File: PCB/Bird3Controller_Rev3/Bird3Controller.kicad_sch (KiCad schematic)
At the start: 61 parts, among them IC1 M24C08-RMN6TP, IC2 AP63203WU-7, J1 Bird 3 24-pin Connector, J2 TXW154028S0 Connector, J3 87832-2220, Q1 2N7002A, SW1 SW_Boot, SW2 SW_Reset, U1 ESP32-S3-WROOM-1, U3 SN65HVD231, U4 LMR36520ADDAR, U5 LM3519MK-20_NOPB

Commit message: Rearrange schematic
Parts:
- J4: value ~ -> Adafruit USB-C Breakout
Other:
- moved on the sheet: C14, C15, C16, C17, C18, C19, C20, C21, C22, C4, C5, C6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

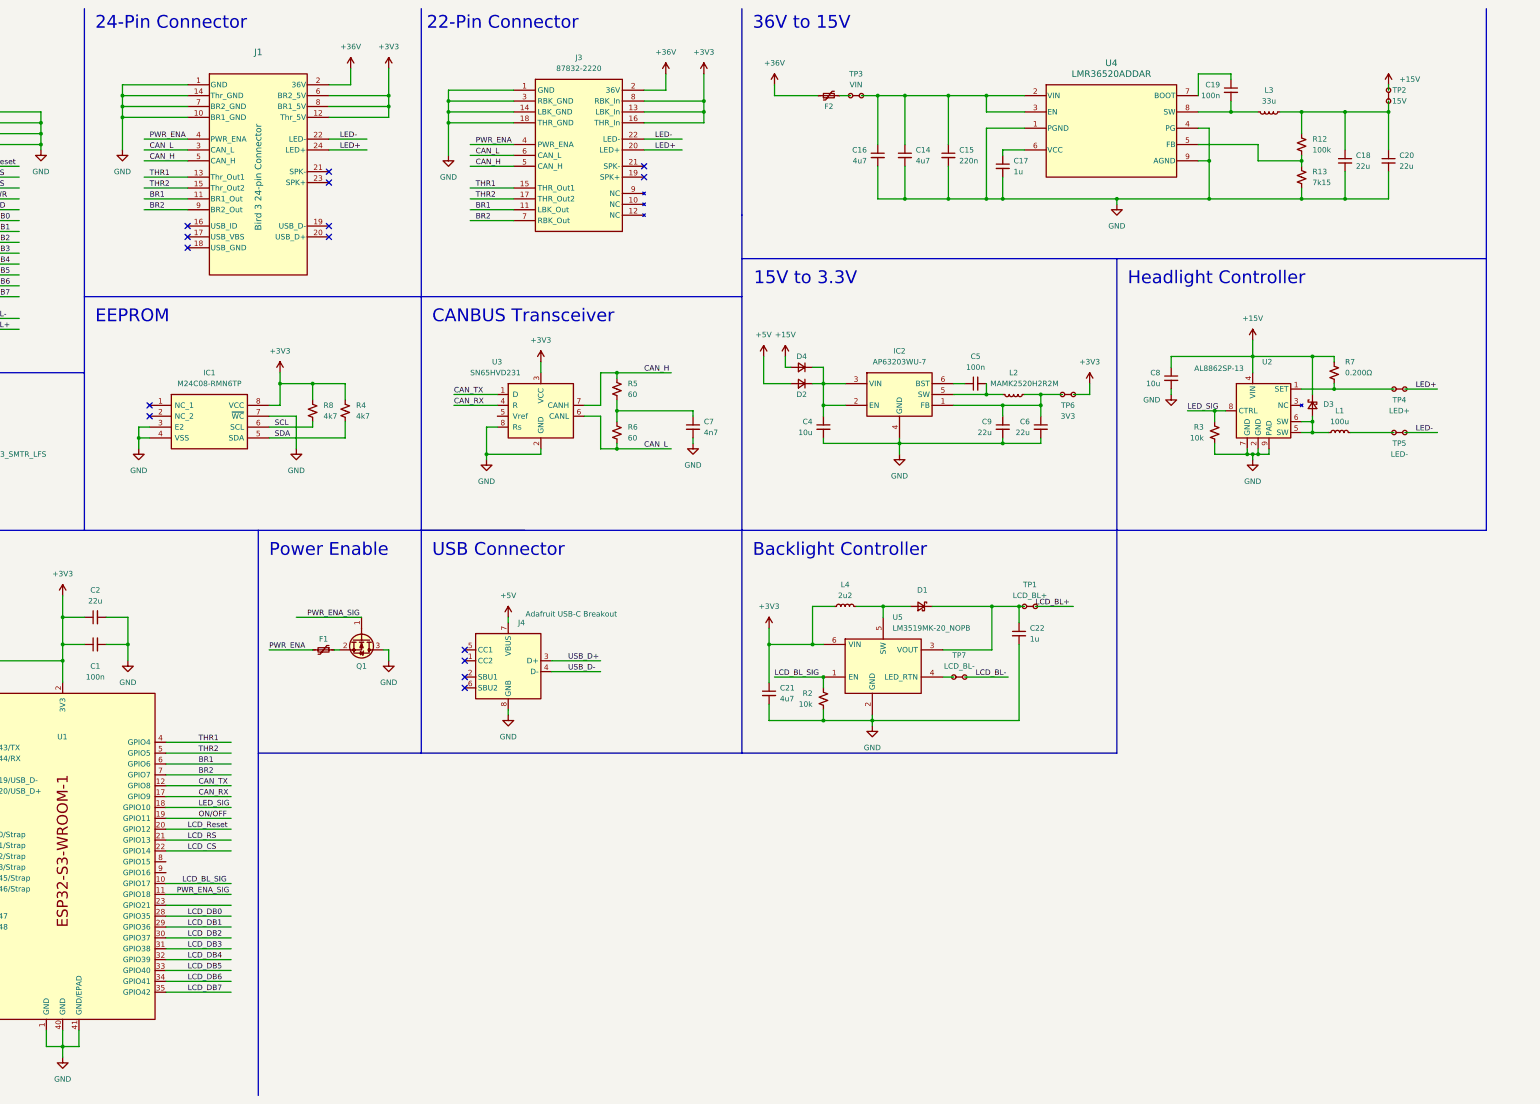
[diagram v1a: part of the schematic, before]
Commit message: Add test points
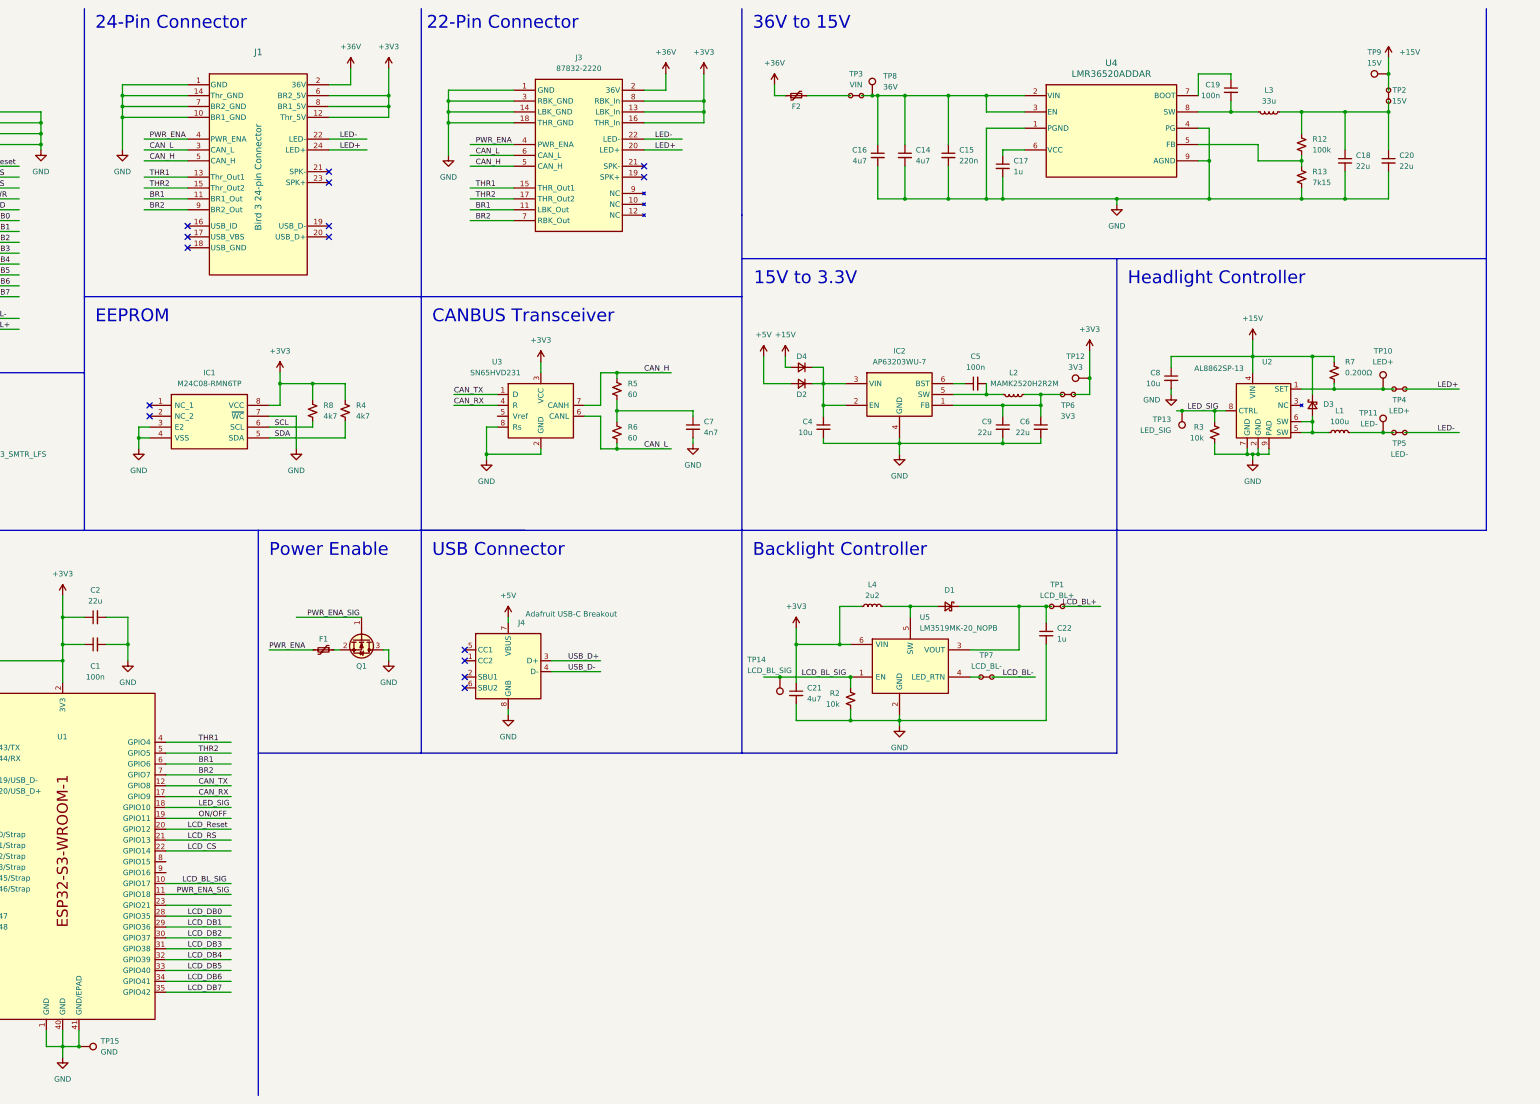
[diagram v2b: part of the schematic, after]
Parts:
- added TP10: LED+, Bird3Controller:Labeled_TestPoint_1.5mm, symbol Connector:TestPoint
- added TP11: LED-, Bird3Controller:Labeled_TestPoint_1.5mm, symbol Connector:TestPoint
- added TP12: 3V3, Bird3Controller:Labeled_TestPoint_1.5mm, symbol Connector:TestPoint
- added TP13: LED_SIG, Bird3Controller:Labeled_TestPoint_1.5mm, symbol Connector:TestPoint
- added TP14: LCD_BL_SIG, Bird3Controller:Labeled_TestPoint_1.5mm, symbol Connector:TestPoint
- added TP15: GND, Bird3Controller:Labeled_TestPoint_1.5mm, symbol Connector:TestPoint
- added TP8: 36V, Bird3Controller:Labeled_TestPoint_1.5mm, symbol Connector:TestPoint
- added TP9: 15V, Bird3Controller:Labeled_TestPoint_1.5mm, symbol Connector:TestPoint
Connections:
- net +15V: now also TP9.1
- net +3V3: now also TP12.1
- net GND: now also TP15.1
- net LCD_BL_SIG: now also TP14.1
- net LED_SIG: now also TP13.1
- net at R7.2, TP4.1, U2.1 (SET): now also TP10.1
- net at L1.2, TP5.1: now also TP11.1
- net at C14.1, C15.1, C16.1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: now also TP8.1
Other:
- moved on the sheet: C21, C22, D1, F2, L4, R2, TP1, TP7, U5

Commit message: Add `Rating` field, use lower cost VIN cap, add description to most components
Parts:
- C1, C17, C19, C22, C3, C5, C7: Rating (none) -> 50V
- C14, C16, C21: Mouser Part Number 187-CL32Y475MCIVPNE -> 187-CL32B475KBUYNNE; Mouser Price QTY1 0.68 -> 0.36; Mouser Price QTY10 0.475 -> 0.179; Mouser Price/Stock https://www.mouser.com/ProductDetail/Samsung-Electro-Mechanics/CL32Y475MCIVPNE?qs=Znm5pLBrcAJ2Wm3glbzndQ%3D%3D -> https://www.mouser.com/ProductDetail/Samsung-Electro-Mechanics/CL32B475KBUYNNE?qs=hqM3L16%252Bxlekel2U%252B66N8g%3D%3D; Rating (none) -> 50V
- C15: Manufacturer_Name KYOCERA AVX -> Samsung Electro-Mechanics; Manufacturer_Part_Number 08053C224K4T4A -> CL21B224KBFNNNG; Mouser Part Number 581-08053C224K4T4A -> 187-CL21B224KBFNNNG; Mouser Price QTY1 0.11 -> 0.10; Mouser Price QTY10 0.078 -> 0.02; Mouser Price/Stock https://www.mouser.com/ProductDetail/KYOCERA-AVX/08053C224K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 -> https://www.mouser.com/ProductDetail/Samsung-Electro-Mechan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; Rating (none) -> 50V
- C18, C20, C4, C8: Rating (none) -> 25V
- C2: Rating (none) -> 16V
- C6, C9: Rating (none) -> 6.3V
- D1, D3: Rating (none) -> 20V
- D2, D4: Rating (none) -> 600V
- F1, F2, U2: Rating (none) -> 60V
- IC1, U5: Rating (none) -> 5.5V
- IC2: Mouser Price QTY1 (none) -> 0.87; Mouser Price QTY10 (none) -> 0.71; Rating (none) -> 32V
- J1, J3: Rating (none) -> 125V, 2A
- J2: Rating (none) -> 50V, 125mA
- L1: Rating (none) -> 1.2A, 300mOhms
- L2: value MAMK2520H2R2M -> 2u2; Mouser Price QTY1 (none) -> 0.23; Mouser Price QTY10 (none) -> 0.158; Rating (none) -> 2.2A, 90mOhms
- L3: Rating (none) -> 4A, 127.6mOhms
- L4: Rating (none) -> 1.3A, 80mOhms
- Q1: Rating (none) -> 60V, 280mA, 2 Ohms
- R1, R2, R3, R4, R8: Rating (none) -> 150v, 125mW
- R12, R13, R5, R6: Rating (none) -> 150v, 500mW
- R7: Rating (none) -> 125mW
- S1, SW1, SW2: Rating (none) -> 12V, 50mA
- U1, U3: Rating (none) -> 3.6V
- U4: Rating (none) -> 65V

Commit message: Rename fields to work with `kicost`. Also, correct the Mouser Part Number for C15.
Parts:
- C1, C19, C3, C5: Manufacturer_Name YAGEO -> (none); Manufacturer_Part_Number AC0805JRX7R9BB104 -> (none); Mouser Part Number 603-AC0805JX7R9BB104 -> (none); Mouser Price QTY10 0.065 -> 0.037; Mouser Price/Stock https://www.mouser.com/ProductDetail/YAGEO/AC0805JRX7R9BB10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 -> https://www.mouser.com/ProductDetail/KYOCERA-AVX/KGM21NR71H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; manf (none) -> KYOCERA AVX; manf# (none) -> KGM21NR71H104KT; mouser# (none) -> 581-KGM21NR71H104KT
- C14, C16: Manufacturer_Name Samsung Electro-Mechanics -> (none); Manufacturer_Part_Number CL32Y475MCIVPNE -> (none); Mouser Part Number 187-CL32B475KBUYNNE -> (none); manf (none) -> Samsung Electro-Mechanics; manf# (none) -> CL21B105KBFNNNE; mouser# (none) -> 187-CL32B475KBUYNNE
- C15: Manufacturer_Name Samsung Electro-Mechanics -> (none); Manufacturer_Part_Number CL21B224KBFNNNG -> (none); Mouser Part Number 187-CL21B224KBFNNNG -> (none); manf (none) -> Samsung Electro-Mechanics; manf# (none) -> CL21B224KBFNNNG; mouser# (none) -> 187-CL21B224KBFNNNG
- C17, C22: Manufacturer_Name Samsung Electro-Mechanics -> (none); Manufacturer_Part_Number CL21B105MBFNNNE -> (none); Mouser Part Number 187-CL21B105MBFNNNE -> (none); Mouser Price QTY1 0.10 -> 0.11; Mouser Price QTY10 0.027 -> 0.045; Mouser Price/Stock https://www.mouser.com/ProductDetail/Samsung-Electro-Mechanics/CL21B105MBFNNNE?qs=Znm5pLBrcAIRYa0zX3s5Qw%3D%3D -> https://www.mouser.com/ProductDetail/Samsung-Electro-Mechanics/CL21B105KBFNNNE?qs=yOVawPpwOwmddQEBPU6Y9A%3D%3D; manf (none) -> Samsung Electro-Mechanics; manf# (none) -> CL21B105KBFNNNE; mouser# (none) -> 187-CL21B105KBFNNNE
- C18, C20: Manufacturer_Name Samsung Electro-Mechanics -> (none); Manufacturer_Part_Number CL21A226MAYNNNE -> (none); Mouser Part Number 187-CL21A226MAYNNNE -> (none); Mouser Price QTY1 0.25 -> 0.32; Mouser Price QTY10 0.115 -> 0.145; manf (none) -> Samsung Electro-Mechanics; manf# (none) -> CL21A226MAYNNWE; mouser# (none) -> 187-CL21A226MAYNNWE
- C2: Manufacturer_Name Murata Electronics -> (none); Manufacturer_Part_Number GRT21BR61C226ME13L -> (none); Mouser Part Number 81-GRT21BR61C226ME3L -> (none); manf (none) -> Murata Electronics; manf# (none) -> GRT21BR61C226ME13L; mouser# (none) -> 81-GRT21BR61C226ME3L
- C21: Manufacturer_Name Samsung Electro-Mechanics -> (none); Manufacturer_Part_Number CL32Y475MCIVPNE -> (none); Mouser Part Number 187-CL32B475KBUYNNE -> (none); manf (none) -> Samsung Electro-Mechanics; manf# (none) -> CL32B475KBUYNNE; mouser# (none) -> 187-CL32B475KBUYNNE
- C4, C8: Manufacturer_Name Murata Electronics -> (none); Manufacturer_Part_Number GRT21BC71E106KE13L -> (none); Mouser Part Number 81-GRT21BC71E106KE13 -> (none); manf (none) -> Murata Electronics; manf# (none) -> GRT21BC71E106KE13L; mouser# (none) -> 81-GRT21BC71E106KE13
- C6, C9: Manufacturer_Name Samsung Electro-Mechanics -> (none); Manufacturer_Part_Number CL21A226MQQNNNE -> (none); Mouser Part Number 187-CL21A226MQQNNNE -> (none); manf (none) -> Samsung Electro-Mechanics; manf# (none) -> CL21A226MQQNNNE; mouser# (none) -> 187-CL21A226MQQNNNE
- C7: Manufacturer_Name KYOCERA AVX -> (none); Manufacturer_Part_Number 08055C472K4T4A -> (none); Mouser Part Number 581-08055C472K4T4A -> (none); manf (none) -> KYOCERA AVX; manf# (none) -> 08055C472K4T4A; mouser# (none) -> 581-08055C472K4T4A
- D1, D3: Manufacturer_Name KYOCERA AVX -> (none); Manufacturer_Part_Number SD0805S020S1R0 -> (none); Mouser Part Number 581-SD0805S020S1R0 -> (none); manf (none) -> KYOCERA AVX; manf# (none) -> SD0805S020S1R0; mouser# (none) -> 581-SD0805S020S1R0
- D2, D4: Manufacturer_Name PANJIT -> (none); Manufacturer_Part_Number GS1J_R1_00001 -> (none); Mouser Part Number 241-GS1J_R1_00001 -> (none); manf (none) -> PANJIT; manf# (none) -> GS1J_R1_00001; mouser# (none) -> 241-GS1J_R1_00001
- F1: Manufacturer_Name Bel Fuse -> (none); Manufacturer_Part_Number 0ZCM0001FF2G -> (none); Mouser Part Number 530-0ZCM0001FF2G -> (none); manf (none) -> Bel Fuse; manf# (none) -> 0ZCM0001FF2G; mouser# (none) -> 530-0ZCM0001FF2G
- F2: Manufacturer_Name BelFuse -> (none); Manufacturer_Part_Number 0ZCF0100AF2A -> (none); Mouser Part Number 530-0ZCF0100AF2A -> (none); manf (none) -> BelFuse; manf# (none) -> 0ZCF0100AF2A; mouser# (none) -> 530-0ZCF0100AF2A
- IC1: Manufacturer_Name STMicroelectronics -> (none); Manufacturer_Part_Number M24C08-RMN6TP -> (none); Mouser Part Number 511-M24C08-RMN6TP -> (none); manf (none) -> STMicroelectronics; manf# (none) -> M24C08-RMN6TP; mouser# (none) -> 511-M24C08-RMN6TP
- IC2: Manufacturer_Name Diodes Incorporated -> (none); Manufacturer_Part_Number AP63203WU-7 -> (none); Mouser Part Number 621-AP63203WU-7 -> (none); manf (none) -> Diodes Incorporated; manf# (none) -> AP63203WU-7; mouser# (none) -> 621-AP63203WU-7
- J1: Manufacturer_Name Molex -> (none); Manufacturer_Part_Number 87832-6123 -> (none); Mouser Part Number 538-87832-6123 -> (none); manf (none) -> Molex; manf# (none) -> 87832-6123; mouser# (none) -> 538-87832-6123
- J2: Manufacturer_Name Hirose -> (none); Manufacturer_Part_Number FH34SRJ-30S-0.5SH(50) -> (none); Mouser Part Number 798-FH34SRJ30S05SH50 -> (none); manf (none) -> Hirose; manf# (none) -> FH34SRJ-30S-0.5SH(50); mouser# (none) -> 798-FH34SRJ30S05SH50
- J3: Manufacturer_Name Molex -> (none); Manufacturer_Part_Number 87832-6062 -> (none); Mouser Part Number 538-87832-6062 -> (none); manf (none) -> Molex; manf# (none) -> 87832-6062; mouser# (none) -> 538-87832-6062
- J4: Manufacturer_Name Adafruit -> (none); Manufacturer_Part_Number 4090 -> (none); Mouser Part Number 485-4090 -> (none); manf (none) -> Adafruit; manf# (none) -> 4090; mouser# (none) -> 485-4090
- L1: Manufacturer_Name Bourns -> (none); Manufacturer_Part_Number SRR1240-101M -> (none); Mouser Part Number 652-SRR1240-101M -> (none); manf (none) -> Bourns; manf# (none) -> SRR1240-101M; mouser# (none) -> 652-SRR1240-101M
- L2: Manufacturer_Name TAIYO YUDEN -> (none); Manufacturer_Part_Number MAMK2520H2R2M -> (none); Mouser Part Number 963-MAMK2520H2R2M -> (none); manf (none) -> TAIYO YUDEN; manf# (none) -> MAMK2520H2R2M; mouser# (none) -> 963-MAMK2520H2R2M
- L3: Manufacturer_Name Bourns -> (none); Manufacturer_Part_Number SRP7050WA-330M -> (none); Mouser Part Number 652-SRP7050WA-330M -> (none); manf (none) -> Bourns; manf# (none) -> SRP7050WA-330M; mouser# (none) -> 652-SRP7050WA-330M
- L4: Manufacturer_Name Bourns -> (none); Manufacturer_Part_Number CVH252009-2R2M -> (none); Mouser Part Number 652-CVH252009-2R2M -> (none); manf (none) -> Bourns; manf# (none) -> CVH252009-2R2M; mouser# (none) -> 652-CVH252009-2R2M
- Q1: Manufacturer_Name Diotec -> (none); Manufacturer_Part_Number 2N7002A -> (none); Mouser Part Number 637-2N7002A -> (none); manf (none) -> Diotec; manf# (none) -> 2N7002A; mouser# (none) -> 637-2N7002A
- R1, R4, R8: Manufacturer_Name Vishay / Dale -> (none); Manufacturer_Part_Number CRCW08054K70JNEA -> (none); Mouser Part Number 71-CRCW0805J-4.7K-E3 -> (none); manf (none) -> Vishay / Dale; manf# (none) -> CRCW08054K70JNEA; mouser# (none) -> 71-CRCW0805J-4.7K-E3
- R12: Manufacturer_Name Vishay / Dale -> (none); Manufacturer_Part_Number RCS0805100KFKEA -> (none); Mouser Part Number 71-RCS0805100KFKEA -> (none); manf (none) -> Vishay / Dale; manf# (none) -> RCS0805100KFKEA; mouser# (none) -> 71-RCS0805100KFKEA
- R13: Manufacturer_Name Vishay / Dale -> (none); Manufacturer_Part_Number CRCW08057K15FKEAC -> (none); Mouser Part Number 71-CRCW08057K15FKEAC -> (none); manf (none) -> Vishay / Dale; manf# (none) -> CRCW08057K15FKEAC; mouser# (none) -> 71-CRCW08057K15FKEAC
- R2, R3: Manufacturer_Name Vishay / Dale -> (none); Manufacturer_Part_Number CRCW080510K0JNEA -> (none); Mouser Part Number 71-CRCW0805J-10K-E3 -> (none); manf (none) -> Vishay / Dale; manf# (none) -> CRCW080510K0JNEA; mouser# (none) -> 71-CRCW0805J-10K-E3
- R5, R6: Manufacturer_Name Vishay / Dale -> (none); Manufacturer_Part_Number RCS080560R4FKEA -> (none); Mouser Part Number 71-RCS080560R4FKEA -> (none); manf (none) -> Vishay / Dale; manf# (none) -> RCS080560R4FKEA; mouser# (none) -> 71-RCS080560R4FKEA
- R7: Manufacturer_Name TE Connectivity / CGS -> (none); Manufacturer_Part_Number RLC73K2AR20FTDF -> (none); Mouser Part Number 279-RLC73K2AR20FTDF -> (none); manf (none) -> TE Connectivity / CGS; manf# (none) -> RLC73K2AR20FTDF; mouser# (none) -> 279-RLC73K2AR20FTDF
- S1: Manufacturer_Name C & K COMPONENTS -> (none); Manufacturer_Part_Number PTS636 SK43 SMTR LFS -> (none); Mouser Part Number 611-PTS636SK43SMTRLF -> (none); manf (none) -> C & K COMPONENTS; manf# (none) -> PTS636 SK43 SMTR LFS; mouser# (none) -> 611-PTS636SK43SMTRLF
- SW1, SW2: Manufacturer_Name C & K COMPONENTS -> (none); Manufacturer_Part_Number PTS526 SK15 SMTR2 LFS -> (none); Mouser Part Number 611-PTS526SK15SMR2L -> (none); manf (none) -> C & K COMPONENTS; manf# (none) -> PTS526 SK15 SMTR2 LFS; mouser# (none) -> 611-PTS526SK15SMR2L
- U1: Manufacturer_Name Espressif Systems -> (none); Manufacturer_Part_Number ESP32-S3-WROOM-1-N8R8 -> (none); Mouser Part Number 356-EP32S3WROOM1N8R8 -> (none); manf (none) -> Espressif Systems; manf# (none) -> ESP32-S3-WROOM-1-N8R8; mouser# (none) -> 356-EP32S3WROOM1N8R8
- U2: Manufacturer_Name Diodes -> (none); Manufacturer_Part_Number AL8862SP-13 -> (none); Mouser Part Number 621-AL8862SP-13 -> (none); manf (none) -> Diodes; manf# (none) -> AL8862SP-13; mouser# (none) -> 621-AL8862SP-13
- U3: Manufacturer_Name Texas Instruments -> (none); Manufacturer_Part_Number SN65HVD231DRG4 -> (none); Mouser Part Number 595-SN65HVD231DRG4 -> (none); manf (none) -> Texas Instruments; manf# (none) -> SN65HVD231DRG4; mouser# (none) -> 595-SN65HVD231DRG4
- U4: Manufacturer_Name Texas Instruments -> (none); Manufacturer_Part_Number LMR36520ADDAR -> (none); Mouser Part Number 595-LMR36520ADDAR -> (none); manf (none) -> Texas Instruments; manf# (none) -> LMR36520ADDAR; mouser# (none) -> 595-LMR36520ADDAR
- U5: Manufacturer_Name Texas Instruments -> (none); Manufacturer_Part_Number LM3519MK-20/NOPB -> (none); Mouser Part Number 926-LM3519MK-20/NOPB -> (none); manf (none) -> Texas Instruments; manf# (none) -> LM3519MK-20/NOPB; mouser# (none) -> 926-LM3519MK-20/NOPB
